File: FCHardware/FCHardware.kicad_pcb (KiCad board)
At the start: 2 copper layers, 39 x 39 mm, 51 parts, among them J2 JST-4pin, J3 JST-8pin, J4 UJ20-C-H-G-SMT-2A-P16-TR, U1 ICM-42688-P, U2 STM32F405RGTx, U3 USBLC6-2SC6, U4 AP2112K-3.3, U5 TPSM63603

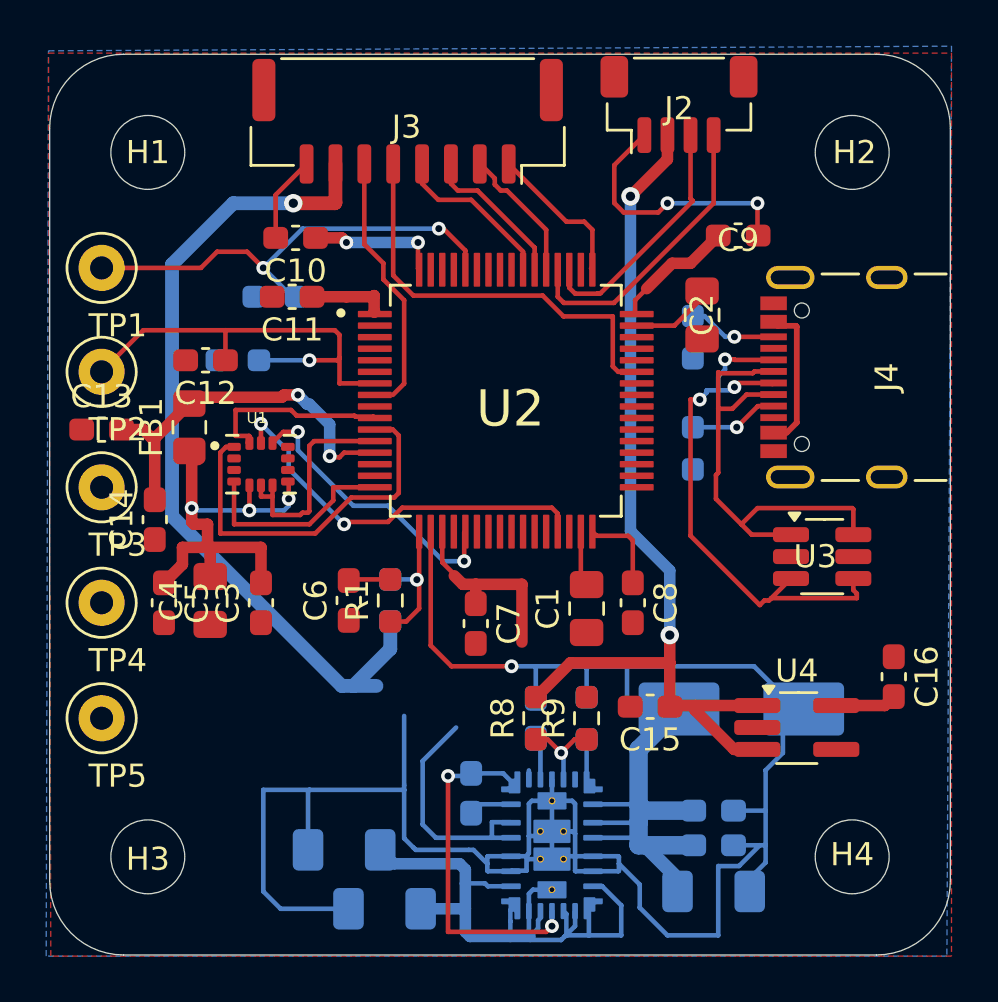
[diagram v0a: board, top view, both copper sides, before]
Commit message: Routed VBAT 5V 3V3
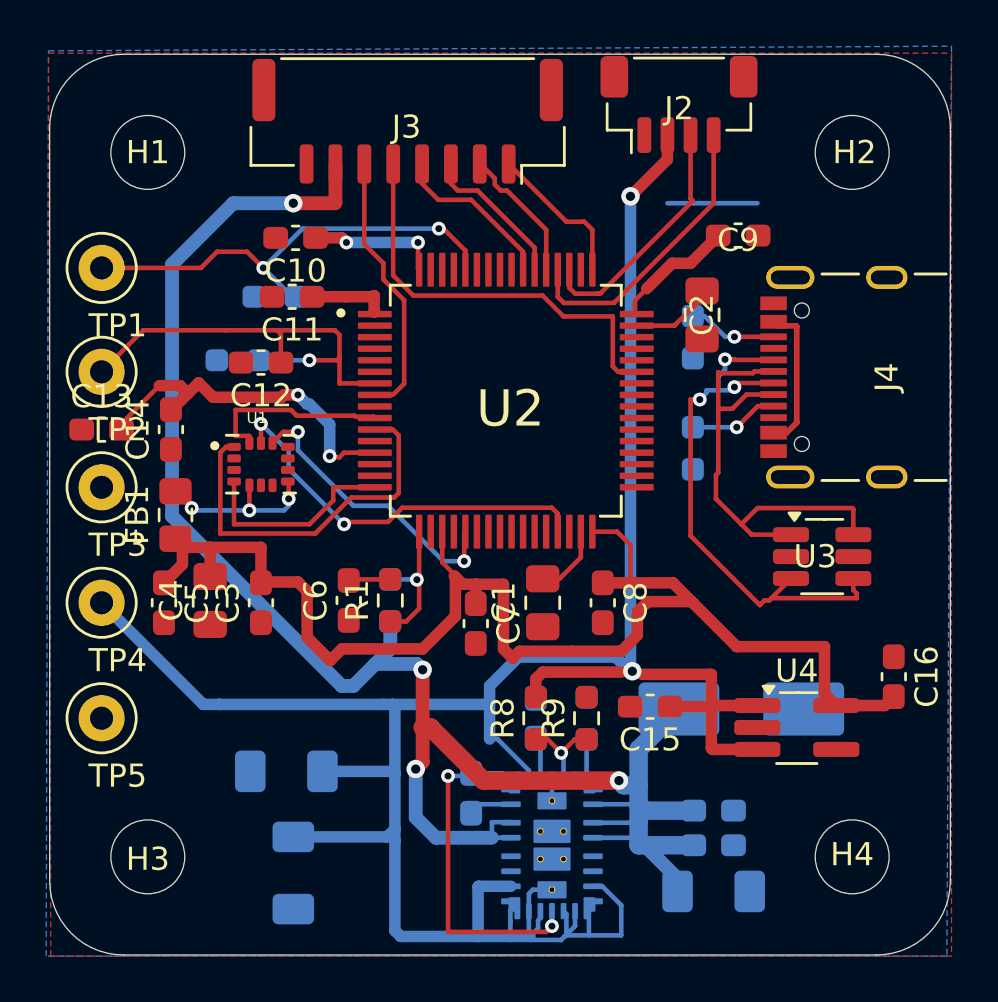
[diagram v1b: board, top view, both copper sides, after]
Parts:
- moved C21 4.24 mm to (90.8, 115.7), turned to -90 degrees
- moved C23 4.22 mm to (90.5, 111.3)
- moved C14 3.96 mm to (85.5, 96.5)
- moved FB1 3.85 mm to (85.7, 100.2)
- moved C12 2.40 mm to (89.4, 93.6)
- moved C1 1.92 mm to (101.6, 104.0)
- moved C8 1.30 mm to (104.2, 104.0)
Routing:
- net GND: track 123.9 -> 4.86 mm, vias 3 -> 0
- net +5V: track 70.0 -> 114.4 mm
- net +3V3: track 49.4 -> 80.3 mm
- net VBAT: track 66.7 -> 80.3 mm, vias 1 -> 4
- net /VDD33A: track 16.6 -> 15.6 mm
- net Net-(U2-VCAP_1): track 2.40 -> 3.15 mm

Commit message: Routed VDD33A and finished VDD33
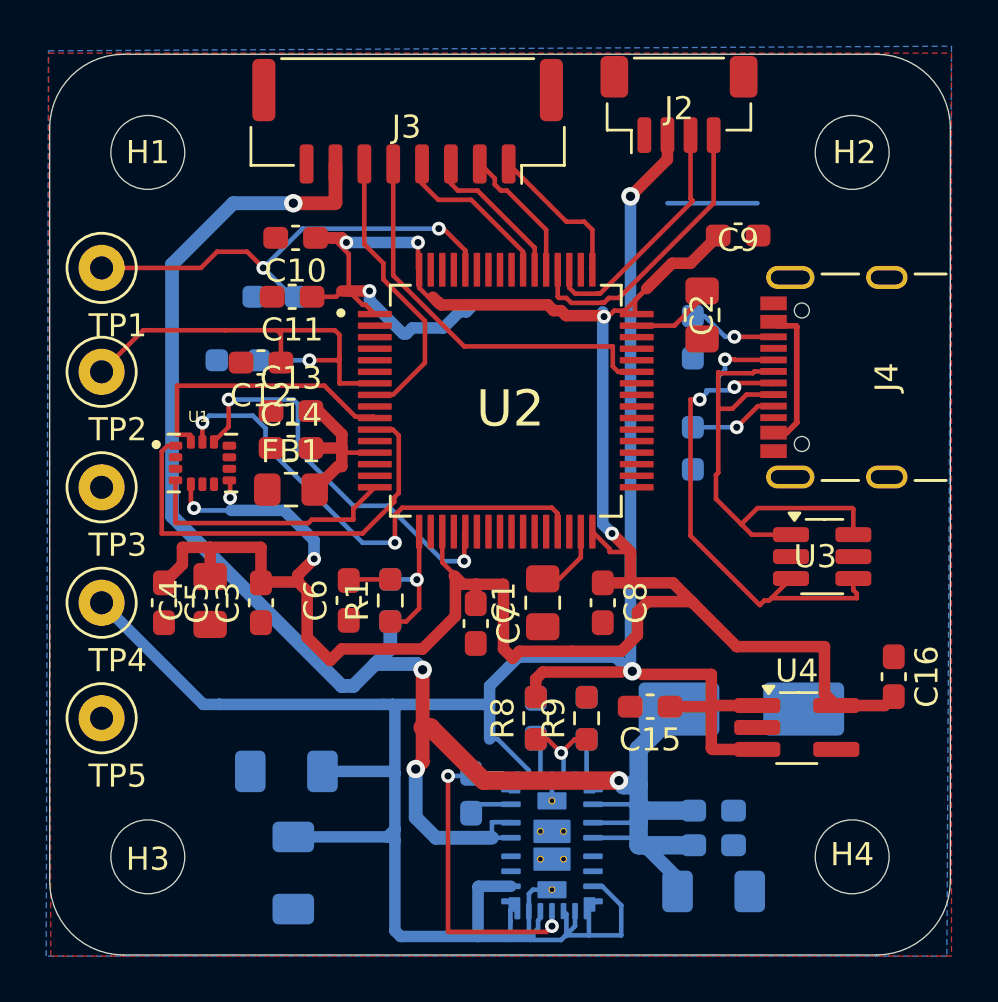
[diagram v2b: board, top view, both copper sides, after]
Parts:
- moved C13 8.24 mm to (90.7, 95.7)
- moved C14 5.26 mm to (90.7, 97.3), turned to 0 degrees
- moved FB1 5.12 mm to (90.7, 99.1), turned to 0 degrees
- moved U1 2.54 mm to (86.9, 98.0)
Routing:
- net +3V3: track 80.3 -> 116.0 mm, vias 5 -> 8
- net /VDD33A: track 15.6 -> 7.59 mm, vias 2 -> 0
- net /IMU_CS: track 12.6 -> 17.7 mm
- net /IMU_SCLK: track 17.3 -> 21.3 mm
- net /IMU_SDI: track 8.35 -> 11.9 mm
- net /IMU_INT: track 8.94 -> 11.4 mm
- net /IMU_SDO: track 16.3 -> 18.6 mm
- net /ESC_TELE: track 18.5 -> 17.8 mm
- net /ESC_CRT: track 10.9 -> 11.7 mm

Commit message: Cleaned up the back routing
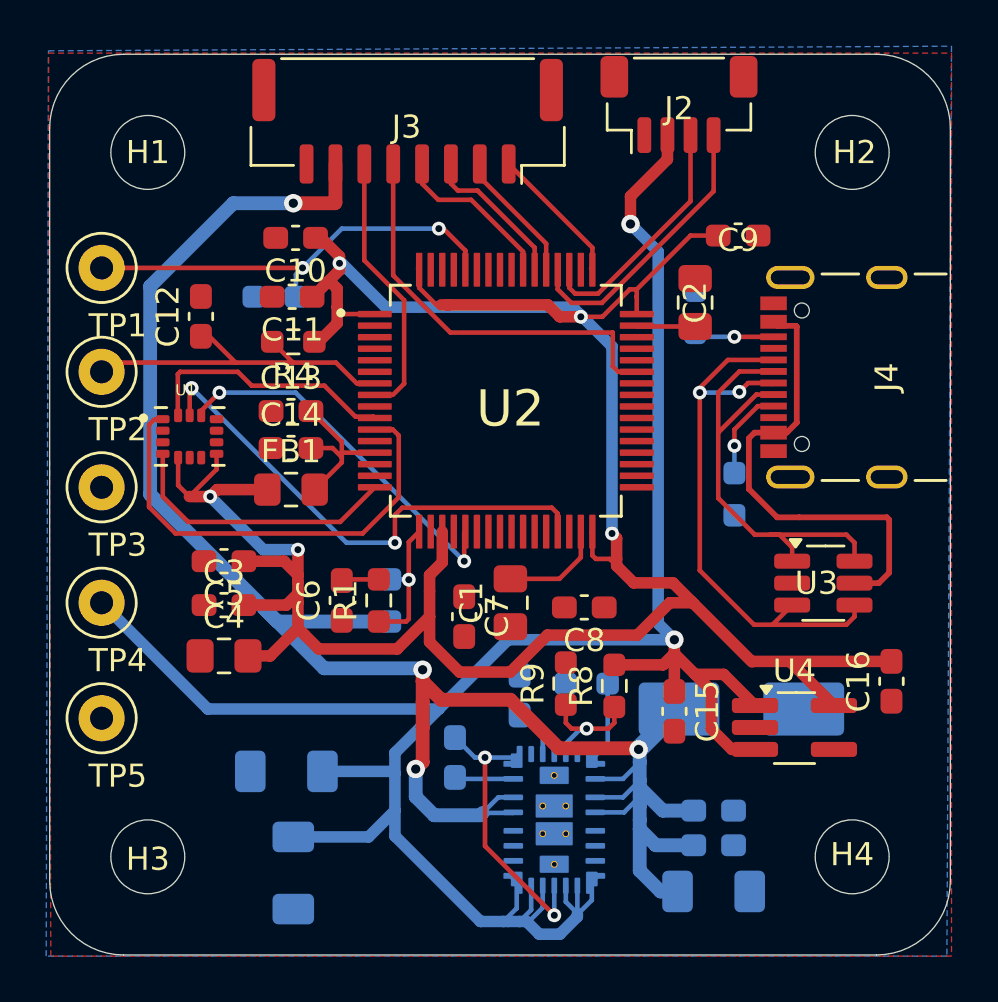
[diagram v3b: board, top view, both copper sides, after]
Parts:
- R4: moved to F.Cu
- moved R8 3.68 mm to (104.7, 107.6)
- moved C12 3.28 mm to (86.8, 91.6), turned to 90 degrees
- moved C5 3.16 mm to (87.8, 102.2), turned to 180 degrees
- moved R10 2.68 mm to (109.9, 99.3)
- moved R4 2.53 mm to (90.8, 92.7), turned to 180 degrees
- moved C4 2.47 mm to (87.8, 106.3), turned to 0 degrees
- moved R9 1.75 mm to (102.6, 107.5)
- moved C22 1.70 mm to (97.8, 110.7)
- moved C3 1.60 mm to (87.8, 104.1), turned to 0 degrees
- moved R7 1.50 mm to (103.5, 107.5), turned to 0 degrees
- moved C1 1.40 mm to (100.2, 104.0)
- moved U1 1.28 mm to (86.3, 96.8)
- moved C20 1.22 mm to (100.6, 108.0)
- moved U3 1.15 mm to (113.8, 103.2)
- moved R11 1.10 mm to (108.2, 91.4), turned to -90 degrees
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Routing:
- net +5V: track 114.4 -> 99.8 mm
- net USB_VBUS: track 6.43 -> 20.4 mm
- net VBAT: track 80.3 -> 85.6 mm
- net GND: track 4.86 -> 0.04 mm
- net /NRST: track 19.8 -> 15.6 mm, vias 1 -> 0
- net /SW: track 15.1 -> 12.8 mm
- net Net-(U5-RT): track 2.01 -> 3.56 mm
- net Net-(U5-FB): track 3.88 -> 5.40 mm
- net /IMU_CS: track 17.7 -> 16.2 mm
- net Net-(U2-VCAP_1): track 3.15 -> 4.55 mm
- net Net-(U2-VCAP_2): track 3.75 -> 2.55 mm
- net /USB_D-: track 20.9 -> 19.9 mm
- net /IMU_SDO: track 18.6 -> 19.7 mm
- net /IMU_SCLK: track 21.3 -> 22.2 mm
- net /USB_D+: track 23.9 -> 24.7 mm, vias 3 -> 2
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
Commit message: Cleaned up the front routing
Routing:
- net +3V3: track 115.9 -> 129.1 mm
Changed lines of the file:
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@@
 	)
 	(segment
-		(start 91.899 105.999)
+		(start 94.4 105.999)
 		(end 95.301 105.999)
 		(width 0.5)
@@
 	)
 	(segment
+		(start 91.899 105.999)
+		(end 94.4 105.999)
+		(width 0.5)
+		(layer "F.Cu")
+		(net 1)
+	)
+	(segment
 		(start 96.7 102.8)
 		(end 97.25 102.25)
@@
 	)
 	(segment
+		(start 82.5 109)
+		(end 91.2 109)
+		(width 0.5)
+		(layer "F.Cu")
+		(net 1)
+	)
+	(segment
 		(start 91 101.7)
 		(end 91 102.8)
@@
 	)
 	(segment
+		(start 91.2 109)
+		(end 94.201 105.999)
+		(width 0.5)
+		(layer "F.Cu")
+		(net 1)
+	)
+	(segment
 		(start 105.67 90.77)
 		(end 105.67 90.73)
@@
 		(start 107.2375 103.1375)
 		(end 105.5375 103.1375)
+		(width 0.5)
+		(layer "F.Cu")
+		(net 1)
+	)
+	(segment
+		(start 94.201 105.999)
+		(end 94.4 105.999)
 		(width 0.5)
 		(layer "F.Cu")
@@
 		(min_thickness 0.2)
 		(filled_areas_thickness no)
-		(fill
+		(fill yes
 			(thermal_gap 0.25)
 			(thermal_bridge_width 0.3)
@@
 		(min_thickness 0.2)
 		(filled_areas_thickness no)
-		(fill
+		(fill yes
 			(thermal_gap 0.25)
 			(thermal_bridge_width 0.3)

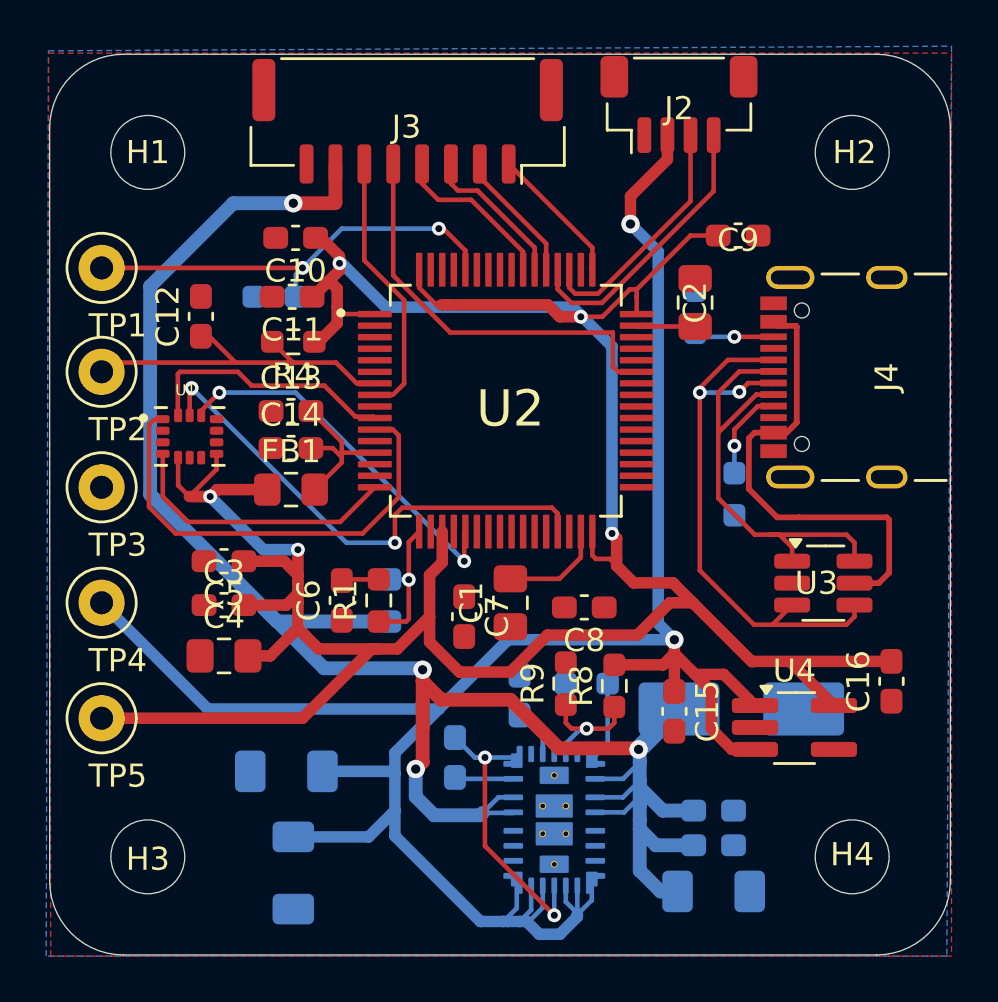
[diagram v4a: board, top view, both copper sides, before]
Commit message: Fixed DRC errors
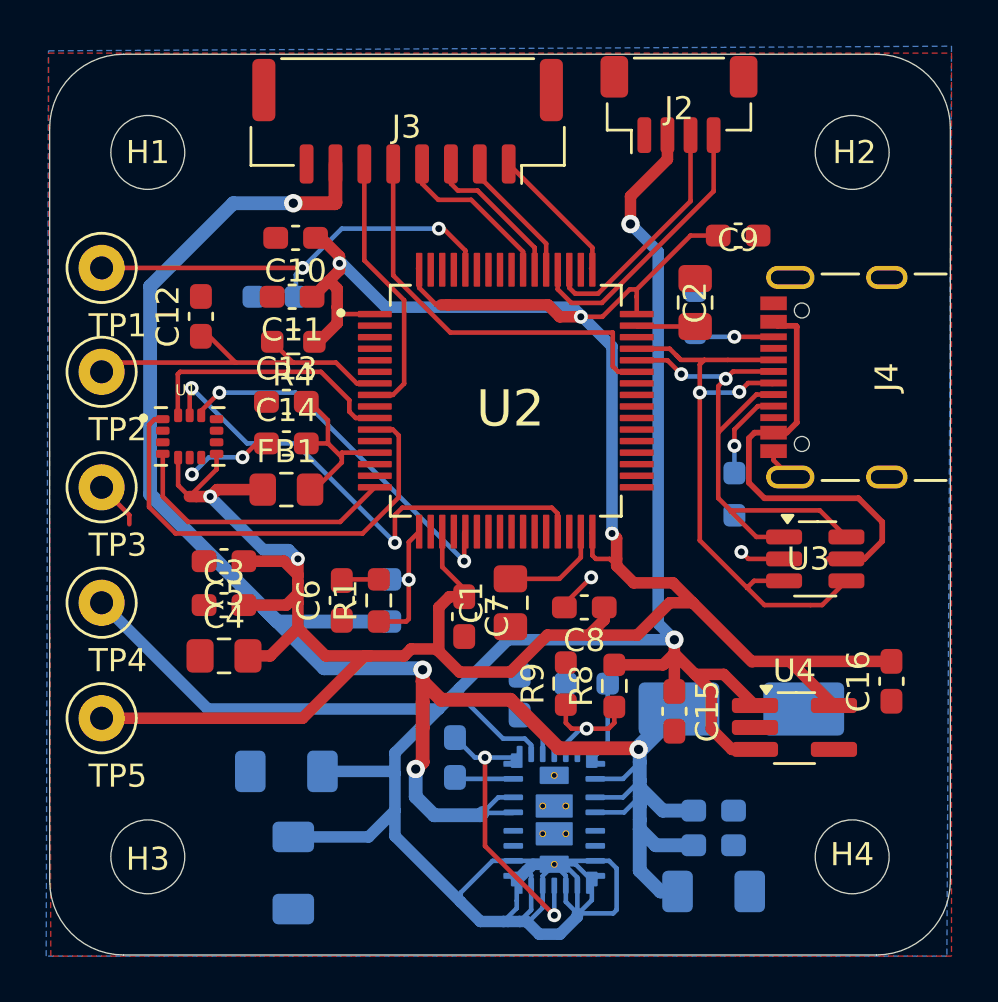
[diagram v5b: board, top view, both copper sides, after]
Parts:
- moved U3 1.11 mm to (113.4, 102.1)
- moved C13 0.45 mm to (90.5, 95.3)
- moved C14 0.28 mm to (90.5, 97.1)
- moved FB1 0.20 mm to (90.5, 99.1)
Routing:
- net +5V: track 99.8 -> 124.5 mm
- net GND: track 0.04 -> 11.1 mm, vias 0 -> 4
- net /USB_D-: track 19.9 -> 24.0 mm, vias 0 -> 2
- net /USB_D+: track 24.7 -> 27.4 mm
- net +3V3: track 129.1 -> 130.8 mm
- net USB_VBUS: track 20.4 -> 19.5 mm
- net /ESC_CRT: track 10.9 -> 11.7 mm
- net /V_MON: track 5.62 -> 6.12 mm
